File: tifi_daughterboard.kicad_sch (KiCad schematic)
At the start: 17 parts

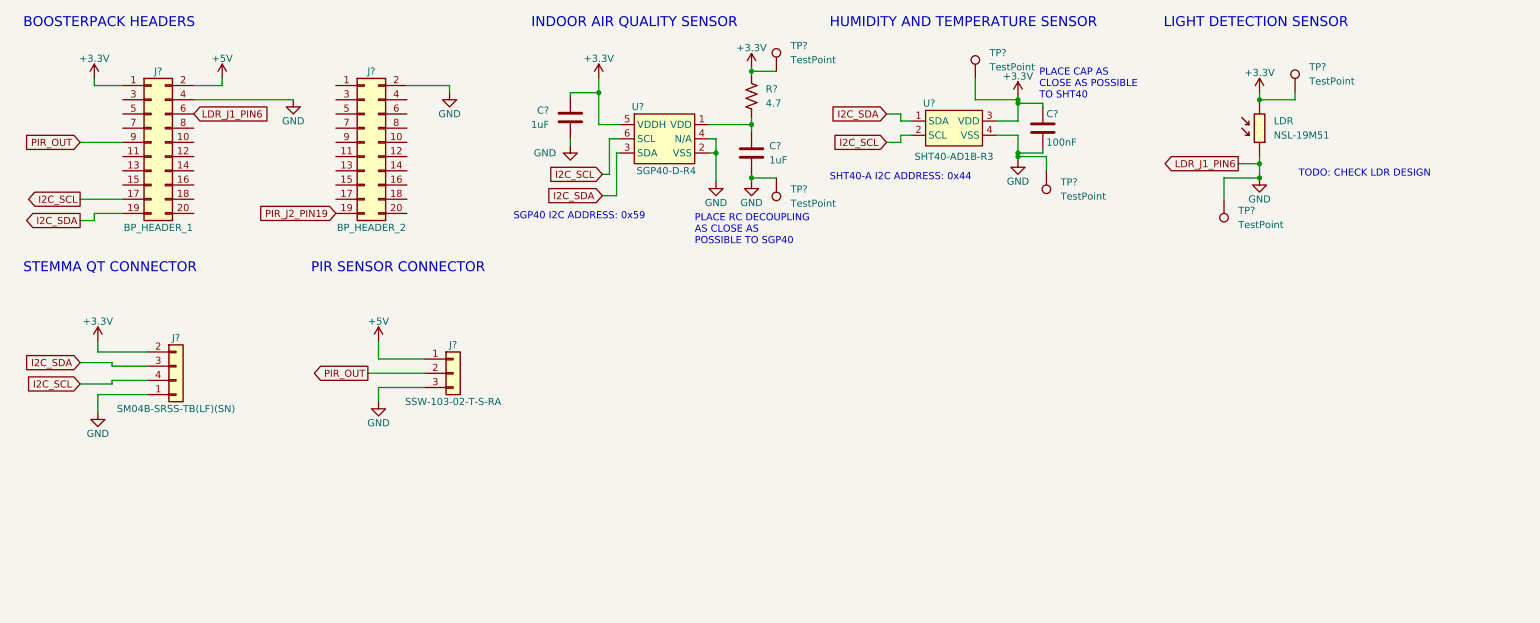
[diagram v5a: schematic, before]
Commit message: Various polish fixes and ADC pin correction.
Removed unused net label.
Added NC flags to headers.
Moved LDR circuit output to ADC pin supported on the CC3220SF LaunchPad.
Update LDR symbol and footprint to use KiCad built-ins.
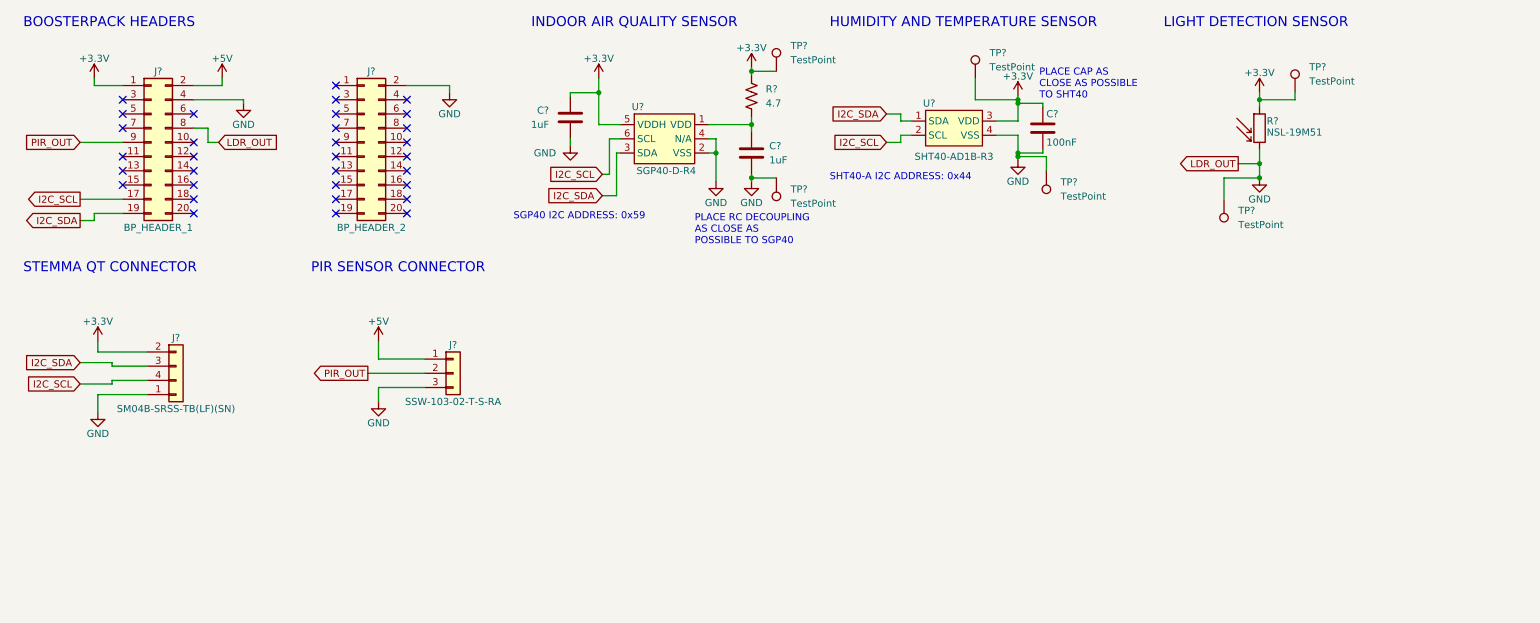
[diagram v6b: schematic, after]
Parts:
- removed LDR: NSL-19M51, New Symbols:NSL_19M51, symbol NSL-19M51:NSL-19M51
- added R?: NSL-19M51, OptoDevice:R_LDR_4.9x4.2mm_P2.54mm_Vertical, symbol Device:R_Photo
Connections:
- net +3.3V: now also R?.1
- net GND: now also J?.8 (Pin_8), R?.2; no longer J?.6 (Pin_6)
- net PIR_J2_PIN19: no longer names the net of J?.19 (Pin_19)
- no-connect marks 0 -> 32
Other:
- note removed: "TODO: CHECK LDR DESIGN"
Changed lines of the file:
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@@
   (junction (at 121.92 31.75) (diameter 0) (color 0 0 0 0)
   )
+  (junction (at 240.03 33.02) (diameter 0) (color 0 0 0 0)
+  )
   (junction (at 240.03 44.45) (diameter 0) (color 0 0 0 0)
   )
@@
   (junction (at 149.225 27.94) (diameter 0) (color 0 0 0 0)
   )
-  (junction (at 240.03 33.02) (diameter 0) (color 0 0 0 0)
-  )
   (junction (at 196.85 42.545) (diameter 0) (color 0 0 0 0)
   )
@@
   (junction (at 149.225 37.465) (diameter 0) (color 0 0 0 0)
   )
+  (no_connect (at 49.53 53.34))
+  (no_connect (at 49.53 50.8))
+  (no_connect (at 74.93 30.48))
+  (no_connect (at 87.63 33.02))
+  (no_connect (at 87.63 35.56))
+  (no_connect (at 74.93 53.34))
+  (no_connect (at 74.93 50.8))
+  (no_connect (at 74.93 48.26))
+  (no_connect (at 74.93 45.72))
+  (no_connect (at 74.93 43.18))
+  (no_connect (at 74.93 40.64))
+  (no_connect (at 74.93 38.1))
+  (no_connect (at 74.93 35.56))
+  (no_connect (at 74.93 33.02))
+  (no_connect (at 87.63 38.1))
+  (no_connect (at 87.63 40.64))
+  (no_connect (at 87.63 43.18))
+  (no_connect (at 87.63 45.72))
+  (no_connect (at 87.63 48.26))
+  (no_connect (at 87.63 50.8))
+  (no_connect (at 87.63 53.34))
+  (no_connect (at 49.53 48.26))
+  (no_connect (at 49.53 45.72))
+  (no_connect (at 49.53 43.18))
+  (no_connect (at 49.53 40.64))
+  (no_connect (at 36.83 33.02))
+  (no_connect (at 36.83 35.56))
+  (no_connect (at 36.83 38.1))
+  (no_connect (at 36.83 43.18))
+  (no_connect (at 36.83 45.72))
+  (no_connect (at 36.83 48.26))
+  (no_connect (at 49.53 35.56))
   (wire (pts (xy 175.895 36.83) (xy 177.8 36.83))
     (stroke (width 0) (type default) (color 0 0 0 0))
@@
     (stroke (width 0) (type default) (color 0 0 0 0))
   )
+  (wire (pts (xy 240.03 33.02) (xy 240.03 34.29))
+    (stroke (width 0) (type default) (color 0 0 0 0))
+  )
   (wire (pts (xy 32.385 78.105) (xy 41.275 78.105))
     (stroke (width 0) (type default) (color 0 0 0 0))
@@
     (stroke (width 0) (type default) (color 0 0 0 0))
   )
-  (wire (pts (xy 49.53 33.02) (xy 67.31 33.02))
+  (wire (pts (xy 49.53 33.02) (xy 58.42 33.02))
     (stroke (width 0) (type default) (color 0 0 0 0))
   )
@@
     (stroke (width 0) (type default) (color 0 0 0 0))
   )
-  (wire (pts (xy 240.03 43.18) (xy 240.03 44.45))
+  (wire (pts (xy 240.03 41.91) (xy 240.03 44.45))
     (stroke (width 0) (type default) (color 0 0 0 0))
   )
@@
     (stroke (width 0) (type default) (color 0 0 0 0))
   )
+  (wire (pts (xy 52.07 38.1) (xy 49.53 38.1))
+    (stroke (width 0) (type default) (color 0 0 0 0))
+  )
   (wire (pts (xy 149.225 46.355) (xy 149.225 46.99))
     (stroke (width 0) (type default) (color 0 0 0 0))
@@
     (stroke (width 0) (type default) (color 0 0 0 0))
   )
+  (wire (pts (xy 53.975 40.64) (xy 52.07 40.64))
+    (stroke (width 0) (type default) (color 0 0 0 0))
+  )
   (wire (pts (xy 34.925 80.645) (xy 41.275 80.645))
     (stroke (width 0) (type default) (color 0 0 0 0))
@@
     (stroke (width 0) (type default) (color 0 0 0 0))
   )
+  (wire (pts (xy 58.42 33.02) (xy 58.42 33.655))
+    (stroke (width 0) (type default) (color 0 0 0 0))
+  )
   (wire (pts (xy 32.385 76.2) (xy 32.385 78.105))
     (stroke (width 0) (type default) (color 0 0 0 0))
@@
     (stroke (width 0) (type default) (color 0 0 0 0))
   )
+  (wire (pts (xy 52.07 40.64) (xy 52.07 38.1))
+    (stroke (width 0) (type default) (color 0 0 0 0))
+  )
   (wire (pts (xy 34.925 83.185) (xy 41.275 83.185))
     (stroke (width 0) (type default) (color 0 0 0 0))
@@
   (wire (pts (xy 31.75 53.34) (xy 31.75 54.61))
     (stroke (width 0) (type default) (color 0 0 0 0))
-  )
-  (text "TODO: CHECK LDR DESIGN" (at 247.015 46.99 0)
-    (effects (font (size 1.27 1.27)) (justify left bottom))
   )
   (text "PLACE RC DECOUPLING\nAS CLOSE AS\nPOSSIBLE TO SGP40" (at 139.065 59.055 0)
@@
     )
   )
-  (global_label "LDR_J1_PIN6" (shape input) (at 49.53 35.56 0) (fields_autoplaced)
+  (global_label "LDR_OUT" (shape input) (at 53.975 40.64 0) (fields_autoplaced)
     (effects (font (size 1.27 1.27)) (justify left))
-    (property "Intersheet References" "${INTERSHEET_REFS}" (id 0) (at 64.0383 35.4806 0)
+    (property "Intersheet References" "${INTERSHEET_REFS}" (id 0) (at 64.5524 40.5606 0)
       (effects (font (size 1.27 1.27)) (justify left) hide)
     )
@@
     )
   )
-  (global_label "PIR_J2_PIN19" (shape input) (at 74.93 53.34 180) (fields_autoplaced)
+  (global_label "LDR_OUT" (shape output) (at 236.22 44.45 180) (fields_autoplaced)
     (effects (font (size 1.27 1.27)) (justify right))
-    (property "Intersheet References" "${INTERSHEET_REFS}" (id 0) (at 59.6355 53.2606 0)
-      (effects (font (size 1.27 1.27)) (justify right) hide)
-    )
-  )
-  (global_label "LDR_J1_PIN6" (shape output) (at 236.22 44.45 180) (fields_autoplaced)
-    (effects (font (size 1.27 1.27)) (justify right))
-    (property "Intersheet References" "${INTERSHEET_REFS}" (id 0) (at 221.7117 44.3706 0)
+    (property "Intersheet References" "${INTERSHEET_REFS}" (id 0) (at 225.6426 44.3706 0)
       (effects (font (size 1.27 1.27)) (justify right) hide)
     )
@@
     (pin "1")
   )
-  (symbol (lib_id "power:GND") (at 67.31 33.02 0) (unit 1)
-    (in_bom yes) (on_board yes)
-    (property "Reference" "#PWR0112" (id 0) (at 67.31 39.37 0)
-      (effects (font (size 1.27 1.27)) hide)
-    )
-    (property "Value" "GND" (id 1) (at 67.31 36.83 0))
-    (property "Footprint" "" (id 2) (at 67.31 33.02 0)
-      (effects (font (size 1.27 1.27)) hide)
-    )
-    (property "Datasheet" "" (id 3) (at 67.31 33.02 0)
-      (effects (font (size 1.27 1.27)) hide)
-    )
-    (pin "1")
-  )
-  (symbol (lib_id "NSL-19M51:NSL-19M51") (at 240.03 38.1 90) (unit 1)
-    (in_bom yes) (on_board yes) (fields_autoplaced)
-    (property "Reference" "LDR" (id 0) (at 242.57 36.8299 90)
-      (effects (font (size 1.27 1.27)) (justify right))
-    )
-    (property "Value" "NSL-19M51" (id 1) (at 242.57 39.3699 90)
-      (effects (font (size 1.27 1.27)) (justify right))
-    )
-    (property "Footprint" "New Symbols:NSL_19M51" (id 2) (at 240.03 38.1 0)
-      (effects (font (size 1.27 1.27)) (justify left bottom) hide)
-    )
-    (property "Datasheet" "" (id 3) (at 240.03 38.1 0)
-      (effects (font (size 1.27 1.27)) (justify left bottom) hide)
-    )
-    (pin "1")
-    (pin "2")
+  (symbol (lib_id "power:GND") (at 58.42 33.655 0) (unit 1)
+    (in_bom yes) (on_board yes)
+    (property "Reference" "#PWR0112" (id 0) (at 58.42 40.005 0)
+      (effects (font (size 1.27 1.27)) hide)
+    )
+    (property "Value" "GND" (id 1) (at 58.42 37.465 0))
+    (property "Footprint" "" (id 2) (at 58.42 33.655 0)
+      (effects (font (size 1.27 1.27)) hide)
+    )
+    (property "Datasheet" "" (id 3) (at 58.42 33.655 0)
+      (effects (font (size 1.27 1.27)) hide)
+    )
+    (pin "1")
   )
   (symbol (lib_id "Device:R_US") (at 149.225 32.385 0) (unit 1)
@@
     (pin "9")
   )
+  (symbol (lib_id "Device:R_Photo") (at 240.03 38.1 0) (unit 1)
+    (in_bom yes) (on_board yes)
+    (property "Reference" "R?" (id 0) (at 241.3 36.83 0)
+      (effects (font (size 1.27 1.27)) (justify left))
+    )
+    (property "Value" "NSL-19M51" (id 1) (at 241.3 38.1 0)
+      (effects (font (size 1.27 1.27)) (justify left top))
+    )
+    (property "Footprint" "OptoDevice:R_LDR_4.9x4.2mm_P2.54mm_Vertical" (id 2) (at 241.3 44.45 90)
+      (effects (font (size 1.27 1.27)) (justify left) hide)
+    )
+    (property "Datasheet" "https://media.digikey.com/pdf/Data%20Sheets/Photonic%20Detetectors%20Inc%20PDFs/NSL-19M51_rev01-04-16.pdf" (id 3) (at 240.03 39.37 0)
+      (effects (font (size 1.27 1.27)) hide)
+    )
+    (pin "1")
+    (pin "2")
+  )
   (symbol (lib_id "power:+3.3V") (at 31.75 29.21 0) (unit 1)
     (in_bom yes) (on_board yes)
@@
       (reference "J?") (unit 1) (value "BP_HEADER_1") (footprint "Connector_PinHeader_2.54mm:PinHeader_2x10_P2.54mm_Vertical")
     )
-    (path "/6e3170e0-2cfe-409f-b8c1-c7618fd99f0e"
-      (reference "LDR") (unit 1) (value "NSL-19M51") (footprint "New Symbols:NSL_19M51")
-    )
     (path "/71672d3b-4690-4212-bfa4-42f5ad120dbb"
       (reference "R?") (unit 1) (value "4.7") (footprint "")
     )
+    (path "/f5356d0d-ea25-437c-9f9a-3a02cfee54ec"
+      (reference "R?") (unit 1) (value "NSL-19M51") (footprint "OptoDevice:R_LDR_4.9x4.2mm_P2.54mm_Vertical")
+    )
     (path "/2b66efc5-294f-4d39-b50d-600901846134"

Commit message: Add STEMMA QT footprint and attributions.
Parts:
- J?: footprint (none) -> STEMMA_QT:JST_SM04B-SRSS-TB(LF)(SN)
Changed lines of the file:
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@@
     (property "Reference" "J?" (id 0) (at 46.355 75.565 0))
     (property "Value" "SM04B-SRSS-TB(LF)(SN)" (id 1) (at 46.355 88.265 0))
-    (property "Footprint" "" (id 2) (at 46.355 80.645 0)
+    (property "Footprint" "STEMMA_QT:JST_SM04B-SRSS-TB(LF)(SN)" (id 2) (at 46.355 80.645 0)
       (effects (font (size 1.27 1.27)) hide)
     )
@@
     )
     (path "/7b912d29-33dd-4ac7-bc62-fbbca0b985f1"
-      (reference "J?") (unit 1) (value "SM04B-SRSS-TB(LF)(SN)") (footprint "")
+      (reference "J?") (unit 1) (value "SM04B-SRSS-TB(LF)(SN)") (footprint "STEMMA_QT:JST_SM04B-SRSS-TB(LF)(SN)")
     )
     (path "/eec51399-1c9c-497c-8d0a-e34cae999a37"

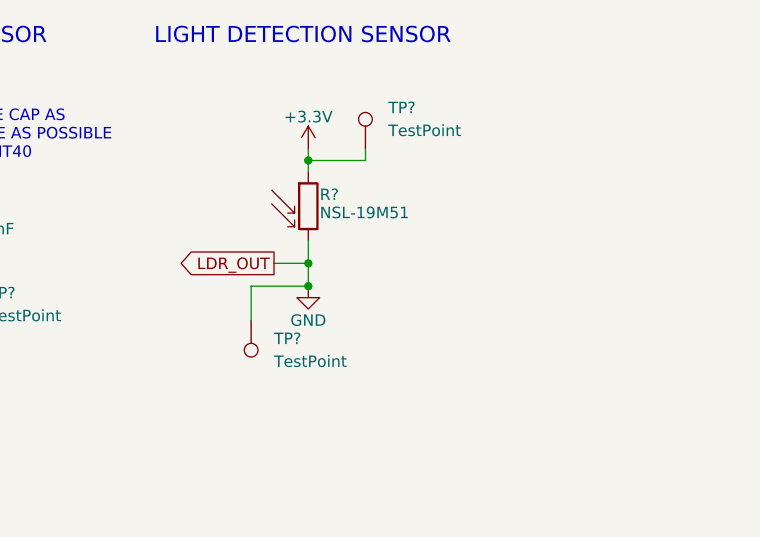
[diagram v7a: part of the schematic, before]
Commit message: Light level sensor fix.
Output was previously obtained from a net connected to GND.
The design now uses a voltage divider.
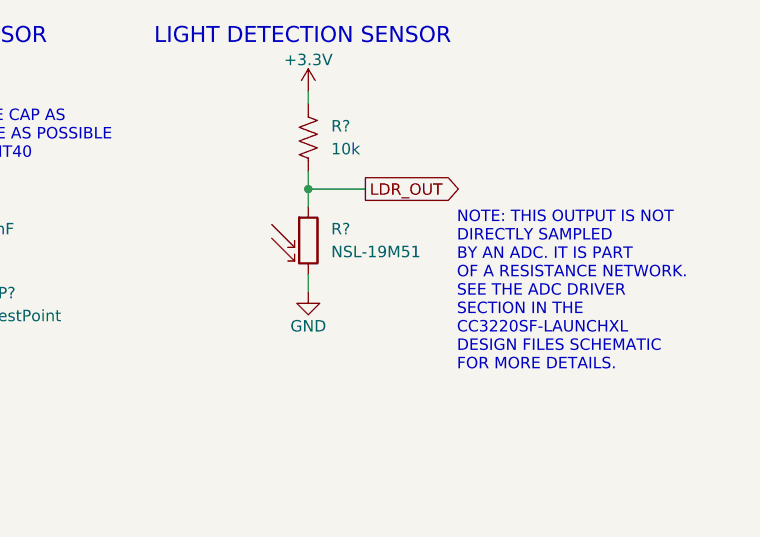
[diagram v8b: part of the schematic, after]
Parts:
- removed TP? (x2): TestPoint, TestPoint:TestPoint_THTPad_1.0x1.0mm_Drill0.5mm, symbol Connector:TestPoint
- added R?: 10k, symbol Device:R_US
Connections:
- net +3.3V: now also R?.1; no longer R?.1
- net GND: no longer J?.8 (Pin_8)
- new net LDR_OUT: J?.8 (Pin_8), R?.1, R?.2
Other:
- note added: "NOTE: THIS OUTPUT IS NOT DIRECTLY SAMPLED BY AN ADC. IT IS PART OF A RESISTANCE NETWORK. SEE THE ADC DRIVER SECTION IN THE CC3220SF-LAUNCHXL DESIGN FILES SCHEMATIC FOR MORE DETAILS."
- moved on the sheet: R?
